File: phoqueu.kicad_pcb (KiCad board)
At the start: 4 copper layers, 212.3 x 75.4 mm, 59 parts, among them J1 18…56 V, J2 On / Off, J3 3.3…24 V, Q1 SiR120DP, Q2 SiR120DP, Q3 SiR120DP, Q4 SiR120DP, SW1 Remote, SW2 Voltage select, T1 320 µ, T2 180 µ, U1 LT4320, U2 i7A4W033A033V

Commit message: Add JLC order number to silkscreen
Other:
- board text added: "JLCJLCJLCJLC"
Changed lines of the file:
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@@
     (effects (font (size 2 2) (thickness 0.25)) (justify mirror))
   )
-  (gr_text "Revision 0" (at 60 129.1) (layer "B.SilkS")
+  (gr_text "JLCJLCJLCJLC" (at 60 129.1) (layer "B.SilkS")
     (effects (font (size 0.85 0.85) (thickness 0.15)) (justify mirror))
   )

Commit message: Add remote control circuit details to silkscreen
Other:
- board text added: "short on open off"
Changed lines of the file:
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@@
     (effects (font (size 2 2) (thickness 0.25)) (justify mirror))
+  )
+  (gr_text "short on\nopen off" (at 61.2 121.9) (layer "B.SilkS")
+    (effects (font (size 1 1) (thickness 0.15)) (justify mirror))
   )
   (gr_text "+" (at 250.125482 89.591902) (layer "B.SilkS")

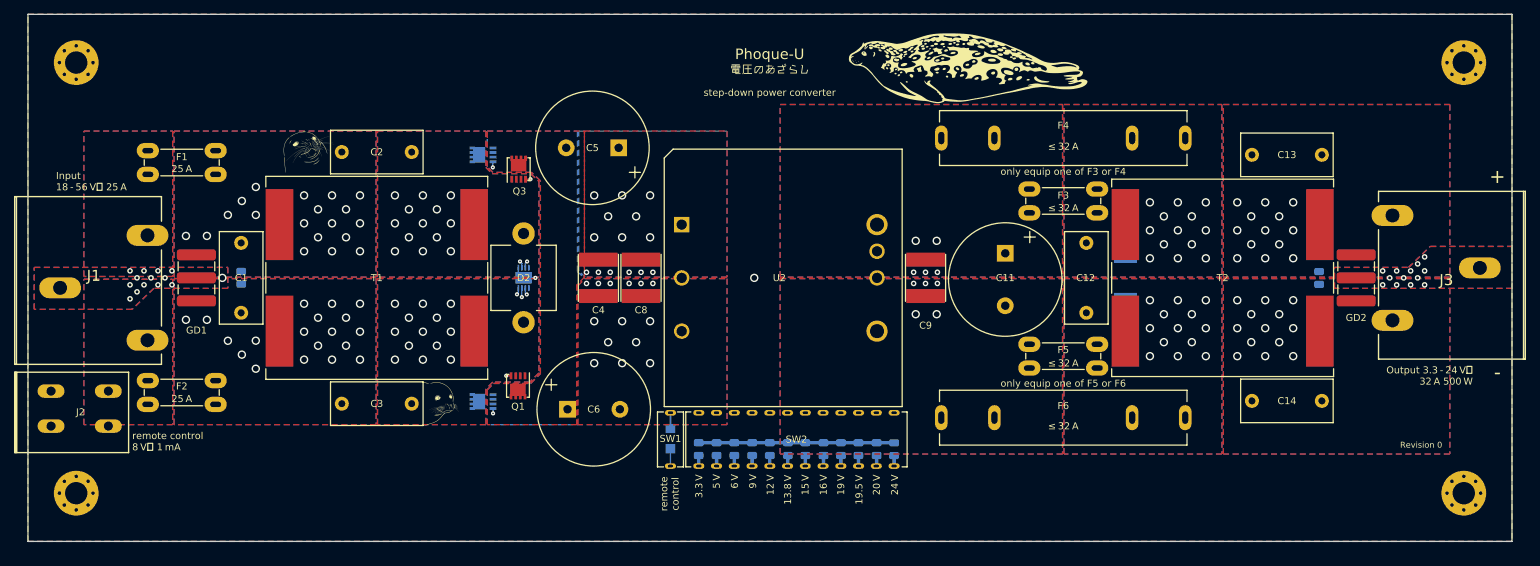
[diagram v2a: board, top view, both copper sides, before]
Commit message: Complete placement and routeing
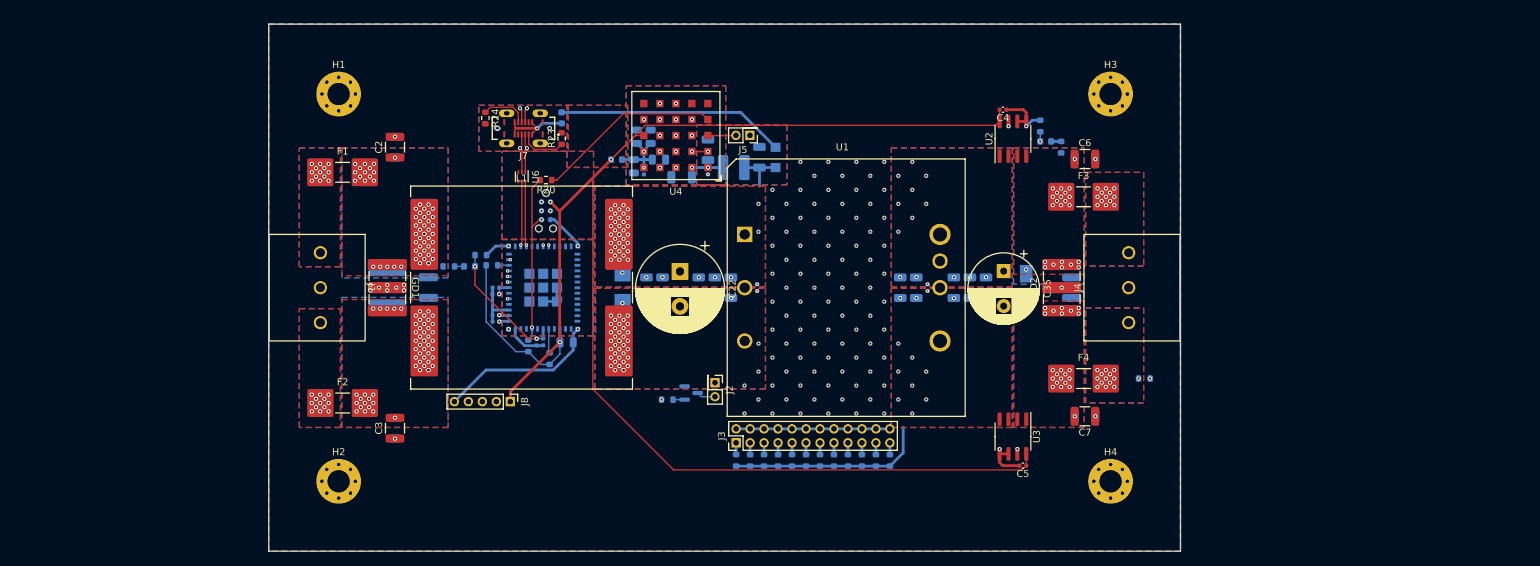
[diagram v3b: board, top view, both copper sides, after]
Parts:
- removed G*** (x3): seal, LOGO
- removed G***: 電圧のあざらし, LOGO
- removed G***: LOGO, LOGO
- removed Q2, Q3, Q4: SiR120DP, Package_SO:Vishay_PowerPAK_1212-8_Single
- removed SW1: Remote, Local:418127160901
- removed SW2: Voltage select, Local:418127160912
- removed T1: 320 µ, Local:CMX1211Z321B-10
- removed T2: 180 µ, Local:CMX1211Z181B-10
- added C10: 4µ7, Capacitor_SMD:C_1206_3216Metric, B.Cu at (136.5, 84.1)
- added C15: 100n, Capacitor_SMD:C_0402_1005Metric, B.Cu at (131.1, 83.2)
- added C16: 4µ7, Capacitor_SMD:C_0805_2012Metric, B.Cu at (120.0, 107.7)
- added C17: 100 n, Capacitor_SMD:C_0402_1005Metric, B.Cu at (109.9, 99.9)
- added C18: 4µ7, Capacitor_SMD:C_0805_2012Metric, B.Cu at (130.1, 78.3)
- added C19: 4µ7, Capacitor_SMD:C_0805_2012Metric, B.Cu at (129.7, 82.5)
- added C20: 4µ7, Capacitor_SMD:C_0805_2012Metric, B.Cu at (132.1, 78.3)
- added C21: 4µ7, Capacitor_SMD:C_0805_2012Metric, B.Cu at (133.3, 81.6)
- added C22: 390 µ, Capacitor_THT:CP_Radial_D12.5mm_P5.00mm, F.Cu at (136.3, 97.6)
- added C23: 4µ7, Capacitor_SMD:C_1206_3216Metric, B.Cu at (131.5, 99.9)
- added C24: 4µ7, Capacitor_SMD:C_1206_3216Metric, B.Cu at (133.8, 99.9)
- added C25: 4µ7, Capacitor_SMD:C_1206_3216Metric, B.Cu at (139.0, 99.9)
- added C26: 4µ7, Capacitor_SMD:C_1206_3216Metric, B.Cu at (141.3, 99.9)
- added C27: 4µ7, Capacitor_SMD:C_1206_3216Metric, B.Cu at (143.6, 99.9)
- added C28: 100n, Capacitor_SMD:C_0402_1005Metric, B.Cu at (147.3, 99.9)
- added C29: 100n, Capacitor_SMD:C_0402_1005Metric, B.Cu at (171.7, 99.9)
- added C30: 4µ7, Capacitor_SMD:C_1206_3216Metric, B.Cu at (175.4, 99.9)
- added C31: 4µ7, Capacitor_SMD:C_1206_3216Metric, B.Cu at (177.8, 99.9)
- added C32: 4µ7, Capacitor_SMD:C_1206_3216Metric, B.Cu at (180.1, 99.9)
- added C33: 4µ7, Capacitor_SMD:C_1206_3216Metric, B.Cu at (170.1, 99.9)
- added C34: 4µ7, Capacitor_SMD:C_1206_3216Metric, B.Cu at (167.8, 99.9)
- added C35: 560 µ, Capacitor_THT:CP_Radial_D10.0mm_P5.00mm, F.Cu at (182.6, 97.5)
- added C7: 4µ7, Capacitor_SMD:C_1210_3225Metric, F.Cu at (194.2, 118.3)
- added D4: 2V5, Diode_SMD:D_0402_1005Metric, B.Cu at (115.8, 107.7)
- added D5: 2V5, Diode_SMD:D_0402_1005Metric, B.Cu at (109.9, 100.8)
- added F7: 500 mA, Fuse:Fuse_0603_1608Metric, B.Cu at (127.2, 81.6)
- added F8: 500 mA, Fuse:Fuse_0603_1608Metric, B.Cu at (119.3, 75.6)
- added J4: 3.3…24 V, phq_Connector:Phoenix_1987737, F.Cu at (200.5, 99.9)
- added J5: MCU disable, Connector_PinHeader_2.00mm:PinHeader_2x01_P2.00mm_Vertical, F.Cu at (146.3, 78.1)
- added J6: TC2030, phq_Connector:TC2030, B.Cu at (117.1, 88.9)
- added J7: USB-C, phq_Connector:USB4120, F.Cu at (113.9, 77.1)
- added J8: I/O, Connector_PinHeader_2.00mm:PinHeader_1x05_P2.00mm_Vertical, F.Cu at (112.0, 116.2)
- added L1: 320µ, phq_SMD:CMX1211Z321B-10, F.Cu at (113.6, 99.9)
- added L2: 15µ, phq_SMD:WE-LQS_4018, B.Cu at (144.0, 82.7)
- added R13: 41R2, Resistor_SMD:R_0603_1608Metric, B.Cu at (166.3, 124.6)
- added R14: 10M, Resistor_SMD:R_0603_1608Metric, B.Cu at (202.7, 112.9)
- added R15: 25M, Resistor_SMD:R_0603_1608Metric, B.Cu at (103.2, 96.9)
- added R16: 1M, Resistor_SMD:R_0603_1608Metric, B.Cu at (107.8, 95.2)
- added R17: 4M7, Resistor_SMD:R_0603_1608Metric, B.Cu at (190.8, 79.8)
- added R18: 500k, Resistor_SMD:R_0603_1608Metric, B.Cu at (187.8, 76.8)
- added R19: 45k3, Resistor_SMD:R_0603_1608Metric, B.Cu at (117.6, 110.1)
- added R20: 0, Resistor_SMD:R_0603_1608Metric, F.Cu at (117.1, 84.5)
- added R21: 45k3, Resistor_SMD:R_0603_1608Metric, B.Cu at (114.6, 108.2)
- added R22: 45k3, Resistor_SMD:R_0603_1608Metric, B.Cu at (109.4, 96.7)
- added R23: 5k1, Resistor_SMD:R_0603_1608Metric, F.Cu at (119.3, 78.6)
- added R24: 5k1, Resistor_SMD:R_0603_1608Metric, F.Cu at (108.4, 75.6)
- added RV3: 85V, Capacitor_SMD:C_1206_3216Metric, B.Cu at (95.5, 120.0)
- added RV4: 85V, Capacitor_SMD:C_1206_3216Metric, B.Cu at (194.2, 81.5)
- added RV5: 85V, Capacitor_SMD:C_1206_3216Metric, B.Cu at (194.2, 118.3)
- added RV6: 24 V, Capacitor_SMD:C_1210_3225Metric, B.Cu at (192.3, 99.9)
- added U3: TMCS1108A1U, Package_SO:SOIC-8_3.9x4.9mm_P1.27mm, F.Cu at (183.9, 121.2)
- added U4: RPMH3.3-0.5, Converter_DCDC:Converter_DCDC_RECOM_RPMx.x-x.0, F.Cu at (135.7, 78.1)
- added U5: ESP32-C3, phq_Module:ESP32-C3-MINI-1U, B.Cu at (116.7, 99.9)
- added U6: ECMF02-2AMX6, Package_DFN_QFN:ST_UQFN-6L_1.5x1.7mm_Pitch0.5mm, F.Cu at (113.6, 84.0)
- C1: value 4n7 -> 4µ7; footprint Local:C_Disc_D13mm_W6.0mm_P10.00mm -> Capacitor_SMD:C_1210_3225Metric; moved to B.Cu
- C11: value 470 µ -> 100n; footprint Local:CP_Radial_D16.0mm_P7.50mm -> Capacitor_SMD:C_0402_1005Metric; moved to B.Cu
- C12, C13, C14: value 4n7 -> 100 n; footprint Local:C_Disc_D13mm_W6.0mm_P10.00mm -> Capacitor_SMD:C_0402_1005Metric; moved to B.Cu
- C2, C3: value 4n7 -> 4µ7; footprint Local:C_Disc_D13mm_W6.0mm_P10.00mm -> Capacitor_SMD:C_1210_3225Metric
- C4: value 22 µ -> 100 n; footprint Local:KRM55WR71J226MH01 -> Capacitor_SMD:C_0402_1005Metric
- C5: value 470 µ -> 100 n; footprint Local:CP_Radial_D16.0mm_P7.50mm -> Capacitor_SMD:C_0402_1005Metric
- C6: value 470 µ -> 4µ7; footprint Local:CP_Radial_D16.0mm_P7.50mm -> Capacitor_SMD:C_1210_3225Metric
- C8, C9: value 22 µ -> 4µ7; footprint Local:KRM55WR71J226MH01 -> Capacitor_SMD:C_1206_3216Metric; moved to B.Cu
- D1: value 8 V -> 54 V; footprint Diode_SMD:D_SMF -> Diode_SMD:D_SMB
- D2: value 56 V -> 24 V; footprint Local:D_BZW50-56B_P12.70mm_Horizontal -> Diode_SMD:D_SMA; moved to B.Cu
- D3: value 24 V -> Schottky diode; footprint Diode_SMD:D_SMC -> Diode_SMD:D_SMF
- F1, F2: value 25 A -> 30 A; footprint Local:3557 -> phq_SMD:Fuse_2410_20A
- F3: value ≤ 32 A -> 30 A; footprint Local:3557 -> phq_SMD:Fuse_2410_20A
- F4: value ≤ 32 A -> 30 A; footprint Local:8040 -> phq_SMD:Fuse_2410_20A
- F5: value ≤ 32 A -> 10 mA; footprint Local:3557 -> Fuse:Fuse_0603_1608Metric; moved to B.Cu
- F6: value ≤ 32 A -> 10 mA; footprint Local:8040 -> Fuse:Fuse_0603_1608Metric; moved to B.Cu
- GD1, GD2: footprint Local:2036-NN-SM -> phq_SMD:2036-NN-SM
- J1: footprint Local:2606-1103 -> phq_Connector:Phoenix_1987737
- J2: value On / Off -> MCU bypass; footprint Local:2604-1102 -> Connector_PinHeader_2.00mm:PinHeader_2x01_P2.00mm_Vertical
- J3: value 3.3…24 V -> Voltage select; footprint Local:2606-1103 -> Connector_PinHeader_2.00mm:PinHeader_2x12_P2.00mm_Vertical
- Q1: value SiR120DP -> NX138AK; footprint Package_SO:Vishay_PowerPAK_1212-8_Single -> Package_TO_SOT_SMD:SOT-23; moved to B.Cu
- R1: value 820k -> 560R; footprint Resistor_SMD:R_0805_2012Metric -> Resistor_SMD:R_0603_1608Metric
- R10: value 261 -> 294; footprint Resistor_SMD:R_0805_2012Metric -> Resistor_SMD:R_0603_1608Metric
- R11: value 232 -> 261; footprint Resistor_SMD:R_0805_2012Metric -> Resistor_SMD:R_0603_1608Metric
- R12: value 41R2 -> 232; footprint Resistor_SMD:R_0805_2012Metric -> Resistor_SMD:R_0603_1608Metric
- R2: value 8k76 -> 820k; footprint Resistor_SMD:R_0805_2012Metric -> Resistor_SMD:R_0603_1608Metric
- R3: value 5k23 -> 8k76; footprint Resistor_SMD:R_0805_2012Metric -> Resistor_SMD:R_0603_1608Metric
- R4: value 2k1 -> 5k23; footprint Resistor_SMD:R_0805_2012Metric -> Resistor_SMD:R_0603_1608Metric
- R5: value 1k13 -> 2k1; footprint Resistor_SMD:R_0805_2012Metric -> Resistor_SMD:R_0603_1608Metric
- R6: value 806 -> 1k13; footprint Resistor_SMD:R_0805_2012Metric -> Resistor_SMD:R_0603_1608Metric
- R7: value 649 -> 806; footprint Resistor_SMD:R_0805_2012Metric -> Resistor_SMD:R_0603_1608Metric
- R8: value 536 -> 649; footprint Resistor_SMD:R_0805_2012Metric -> Resistor_SMD:R_0603_1608Metric
- R9: value 294 -> 536; footprint Resistor_SMD:R_0805_2012Metric -> Resistor_SMD:R_0603_1608Metric
- RV1: footprint Resistor_SMD:R_0805_2012Metric -> Capacitor_SMD:C_2220_5650Metric
- RV2: value 24 V -> 85V; footprint Resistor_SMD:R_0805_2012Metric -> Capacitor_SMD:C_1206_3216Metric
- U1: value LT4320 -> i7A4W033A033V; footprint Package_DFN_QFN:DFN-8-1EP_3x3mm_P0.5mm_EP1.65x2.38mm -> phq_Module:i7A4W-0C1; moved to F.Cu
- U2: value i7A4W033A033V -> TMCS1108A1U; footprint Local:i7A4W033A033V-0C1 -> Package_SO:SOIC-8_3.9x4.9mm_P1.27mm
- moved H2 171.7 mm to (87.4, 127.6)
- moved H3 158.6 mm to (197.9, 72.2)
- moved RV2 133.5 mm to (95.5, 79.8), turned to 90 degrees
- moved C13 115.5 mm to (109.9, 103.8)
- moved C14 106.7 mm to (116.7, 107.7), turned to -90 degrees
- moved J3 106.6 mm to (144.3, 122.1), turned to 90 degrees
- moved J2 95.4 mm to (141.3, 113.5), turned to -90 degrees
- moved F5 85.9 mm to (106.2, 96.9)
- moved C12 84.7 mm to (109.9, 104.8), turned to 180 degrees
- moved C6 82.2 mm to (194.2, 81.5)
- moved C5 73.6 mm to (185.3, 125.4)
- moved D2 71.9 mm to (185.8, 99.9), turned to -90 degrees
- moved C4 62.7 mm to (182.5, 74.4), turned to 180 degrees
- moved D3 52.9 mm to (149.9, 81.3), turned to 90 degrees
- moved H4 50.6 mm to (197.9, 127.6)
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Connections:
- net /V_{in}± renamed /V_{inr}+
- net /V_{in}∓ renamed /V_{inr}-
- C1 pad 1: /V_{infuse}± -> V_{in}
- C1 pad 2: /V_{infuse}∓ -> Net-(C1-Pad2)
- C11 pad 1: /V_{out}+ -> Net-(C10-Pad2)
- C11 pad 2: /V_{out}- -> GND
- C12 pad 1: /V_{outfuse}- -> ESP_AD1_0
- C12 pad 2: /V_{outfuse}+ -> GND
- C13 pad 1: /V_{outfilt}+ -> ESP_AD1_1
- C14 pad 1: GND -> /MCU/ESP_AD1_3
- C14 pad 2: /V_{outfilt}- -> GND
- C2 pad 1: /V_{infilt}± -> V_{in}
- C2 pad 2: GND -> Earth
- C3 pad 1: GND -> Earth
- C3 pad 2: /V_{infilt}∓ -> Net-(C1-Pad2)
- C4 pad 1: /V_{in}+ -> GND
- C4 pad 2: /V_{in}- -> +3V3
- C5 pad 1: /V_{in}+ -> +3V3
- C5 pad 2: /V_{in}- -> GND
- C6 pad 1: /V_{in}+ -> V_{out}
- C6 pad 2: /V_{in}- -> Earth
- C8 pad 1: /V_{in}+ -> GND
- C8 pad 2: /V_{in}- -> +48V
- C9 pad 1: /V_{out}+ -> GND
- C9 pad 2: /V_{out}- -> Net-(C10-Pad2)
- D1 pad 1: /On/Off -> +48V
- D1 pad 2: /V_{in}- -> GND
- D2 pad 1: /V_{infilt}∓ -> V_{out}
- D2 pad 2: /V_{infilt}± -> Net-(C7-Pad2)
- D3 pad 1: /V_{outfuse}+ -> +48V
- D3 pad 2: /V_{outfuse}- -> +5V
- F1 pad 2: /V_{infuse}± -> V_{in}
- F2 pad 2: /V_{infuse}∓ -> Net-(C1-Pad2)
- F3 pad 1: /V_{out}+ -> V_{out}
- F3 pad 2: /V_{outfuse}+ -> /V_{out}+
- F4 pad 1: /V_{out}+ -> Net-(C7-Pad2)
- F4 pad 2: /V_{outfuse}+ -> /V_{out}-
- F5 pad 1: /V_{out}- -> Net-(F5-Pad1)
- F5 pad 2: /V_{outfuse}- -> /MCU/ESP_AD1_3
- F6 pad 1: /V_{out}- -> Net-(F6-Pad1)
- F6 pad 2: /V_{outfuse}- -> /MCU/ESP_AD1_4
- GD1 pad 1: /V_{infuse}± -> V_{in}
- GD1 pad 2: GND -> Earth
- GD1 pad 3: /V_{infuse}∓ -> Net-(C1-Pad2)
- GD2 pad 1: /V_{outfilt}- -> Net-(C7-Pad2)
- GD2 pad 2: GND -> Earth
- GD2 pad 3: /V_{outfilt}+ -> V_{out}
- H1 pad 1: GND -> Earth
- H2 pad 1: GND -> Earth
- H3 pad 1: GND -> Earth
- H4 pad 1: GND -> Earth
- J1 pad 2: GND -> Earth
- J2 pad 1: /On/Off -> GND
- J2 pad 2: /V_{in}- -> Net-(J2-Pad2)
- J3 pad 1: /V_{outfilt}- -> Net-(R2-Pad1)
- J3 pad 2: GND -> /Trim
- J3 pad 3: /V_{outfilt}+ -> Net-(J3-Pad3)
- Q1 pad 1: /V_{infilt}∓ -> Net-(Q1-Pad1)
- Q1 pad 2: /V_{infilt}∓ -> GND
- Q1 pad 3: /V_{infilt}∓ -> Net-(J2-Pad2)
- R1 pad 1: Net-(R1-Pad1) -> ESP_IO10
- R1 pad 2: /V_{out}- -> Net-(Q1-Pad1)
- R10 pad 1: Net-(R10-Pad1) -> Net-(J3-Pad17)
- R10 pad 2: /V_{out}- -> GND
- R11 pad 1: Net-(R11-Pad1) -> Net-(J3-Pad19)
- R11 pad 2: /V_{out}- -> GND
- R12 pad 1: Net-(R12-Pad1) -> Net-(J3-Pad21)
- R12 pad 2: /V_{out}- -> GND
- R2 pad 2: /V_{out}- -> GND
- R3 pad 1: Net-(R3-Pad1) -> Net-(J3-Pad3)
- R3 pad 2: /V_{out}- -> GND
- R4 pad 2: /V_{out}- -> GND
- R5 pad 2: /V_{out}- -> GND
- R6 pad 2: /V_{out}- -> GND
- R7 pad 2: /V_{out}- -> GND
- R8 pad 2: /V_{out}- -> GND
- R9 pad 2: /V_{out}- -> GND
- RV1 pad 1: /V_{infuse}± -> V_{in}
- RV1 pad 2: /V_{infuse}∓ -> Net-(C1-Pad2)
- RV2 pad 1: /V_{outfilt}+ -> V_{in}
- RV2 pad 2: /V_{outfilt}- -> Earth
- U1 pad 1: /V_{infilt}∓ -> +48V
- U1 pad 2: /G_{Q1} -> Net-(J2-Pad2)
- U1 pad 3: /G_{Q2} -> GND
- U1 pad 4: /G_{Q4} -> GND
- U1 pad 6: /V_{in}+ -> /Trim
- U1 pad 7: /G_{Q3} -> V_{out}
- U1 pad 8: /V_{infilt}± -> /Output caps/in+
- U2 pad 1: /V_{in}+ -> /Output caps/in+
- U2 pad 2: /On/Off -> /Output caps/in+
- U2 pad 3: /V_{in}- -> V_{out}
- U2 pad 4: /V_{out}- -> V_{out}
- U2 pad 6: /Trim -> GND
- U2 pad 7: /V_{outfilt}+ -> ESP_AD1_1
- U2 pad 8: /V_{out}+ -> +3V3
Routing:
- net +3V3: track 0.00 -> 236.3 mm, vias 0 -> 3
- net GND: track 0.00 -> 142.3 mm, vias 28 -> 83
- net /On/Off: track 122.2 -> 0.00 mm
- net /V_{in}-: track 113.7 -> 0.00 mm, vias 15 -> 0
- net /MCU/ESP_AD1_4: track 0.00 -> 90.1 mm, vias 0 -> 2
- net ESP_AD1_1: track 0.00 -> 85.4 mm, vias 0 -> 2
- net ESP_AD1_0: track 0.00 -> 84.2 mm, vias 0 -> 2
- net /V_{outfilt}+: track 80.3 -> 0.00 mm, vias 13 -> 0
- net +5V: track 0.00 -> 32.7 mm
- net ESP_IO10: track 0.00 -> 28.0 mm, vias 0 -> 2
- net /V_{out}-: track 27.9 -> 0.00 mm, vias 5 -> 14
- net Net-(R20-Pad1): track 0.00 -> 26.6 mm
- net /MCU/ESP_EN: track 0.00 -> 25.2 mm, vias 0 -> 2
- net /G_{Q2}: track 22.3 -> 0.00 mm, vias 2 -> 0
- net Net-(J2-Pad2): track 0.00 -> 21.1 mm
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- added copper zone on B.Cu, net +48V
- added copper zone on F.Cu, net +48V
- added copper zone on B.Cu, net /Output caps/in+
- added copper zone on F.Cu, net /Output caps/in+
- added copper zone on B.Cu, net Earth
- added copper zone on F.Cu, net Earth
- added copper zone on In1.Cu, net Earth
- added copper zone on In2.Cu, net Earth
- added copper zone on In1.Cu, net GND
- added copper zone on B.Cu, net Net-(C1-Pad2)
- added copper zone on F.Cu, net Net-(C1-Pad2)
- added copper zone on B.Cu, net Net-(C7-Pad2)
- added copper zone on F.Cu, net Net-(C7-Pad2)
- added copper zone on B.Cu, net V_{in}
- added copper zone on F.Cu, net V_{in}
- added copper zone on B.Cu, net V_{out}
- added copper zone on F.Cu, net V_{out}
- removed copper zone on B.Cu, net /V_{infilt}±
- removed copper zone on F.Cu, net /V_{infilt}±
- removed copper zone on B.Cu, net /V_{infilt}∓
- removed copper zone on F.Cu, net /V_{infilt}∓
- removed copper zone on B.Cu, net /V_{infuse}±
- removed copper zone on F.Cu, net /V_{infuse}±
- removed copper zone on B.Cu, net /V_{infuse}∓
- removed copper zone on F.Cu, net /V_{infuse}∓
- removed copper zone on B.Cu, net /V_{in}+
- removed copper zone on F.Cu, net /V_{in}+
- removed copper zone on B.Cu, net /V_{in}-
- removed copper zone on F.Cu, net /V_{in}-
- removed copper zone on B.Cu, net /V_{outfilt}+
- removed copper zone on F.Cu, net /V_{outfilt}+
- removed copper zone on B.Cu, net /V_{outfilt}-
- removed copper zone on F.Cu, net /V_{outfilt}-
- removed copper zone on B.Cu, net /V_{outfuse}+
- removed copper zone on F.Cu, net /V_{outfuse}+
- removed copper zone on B.Cu, net /V_{outfuse}-
- removed copper zone on F.Cu, net /V_{outfuse}-
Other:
- board size 212.3 x 75.4 mm -> 130.4 x 75.4 mm
- board text removed: "+"
- board text removed: "-"
- board text removed: "12 V"
- board text removed: "13.8 V"
- board text removed: "15 V"
- board text removed: "16 V"
- board text removed: "19 V"
- board text removed: "19.5 V"
- board text removed: "20 V"
- board text removed: "24 V"
- board text removed: "25 A"
- board text removed: "3.3 V"
- board text removed: "5 V"
- board text removed: "6 V"
- board text removed: "9 V"
- board text removed: "Designed in 2022 by Mikael Voss This work may be used under the terms of the strictly‐reciprocative CERN Open Hardware Licence (CERN-OHL-S) version 2."
- board text removed: "Input 18 - 56 V⎓ 25 A"
- board text removed: "JLCJLCJLCJLC"
- board text removed: "Output 3.3 - 24 V⎓ 32 A 500 W"
- board text removed: "Phoque-U"
- board text removed: "Revision 0"
- board text removed: "Warum Thunfische das‽"
- board text removed: "only equip one of F3 or F4"
- board text removed: "only equip one of F5 or F6"
- board text removed: "remote control"
- board text removed: "remote control 8 V⎓ 1 mA"
- board text removed: "short on open off"
- board text removed: "step‐down power converter"
- board text removed: "±"
- board text removed: "∓"
- board text removed: "≤ 32 A"
- board text removed: "⏚"
